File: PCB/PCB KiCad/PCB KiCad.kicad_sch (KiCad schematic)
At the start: 0 parts

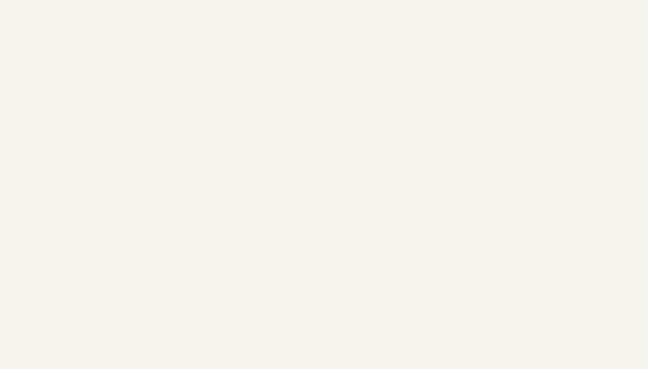
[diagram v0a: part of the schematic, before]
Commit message: draw schematic for 60%
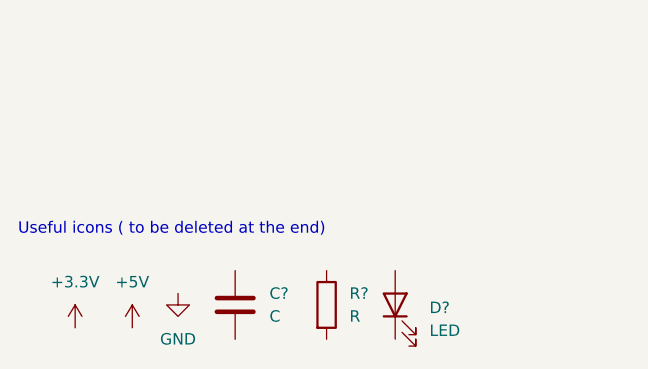
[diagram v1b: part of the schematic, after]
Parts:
- added C?: C, Capacitor_SMD:C_0805_2012Metric_Pad1.18x1.45mm_HandSolder, symbol Device:C
- added D?: LED, symbol Device:LED
- added R?: R, Resistor_SMD:R_0805_2012Metric_Pad1.20x1.40mm_HandSolder, symbol Device:R
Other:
- note added: "Useful icons ( to be deleted at the end)"

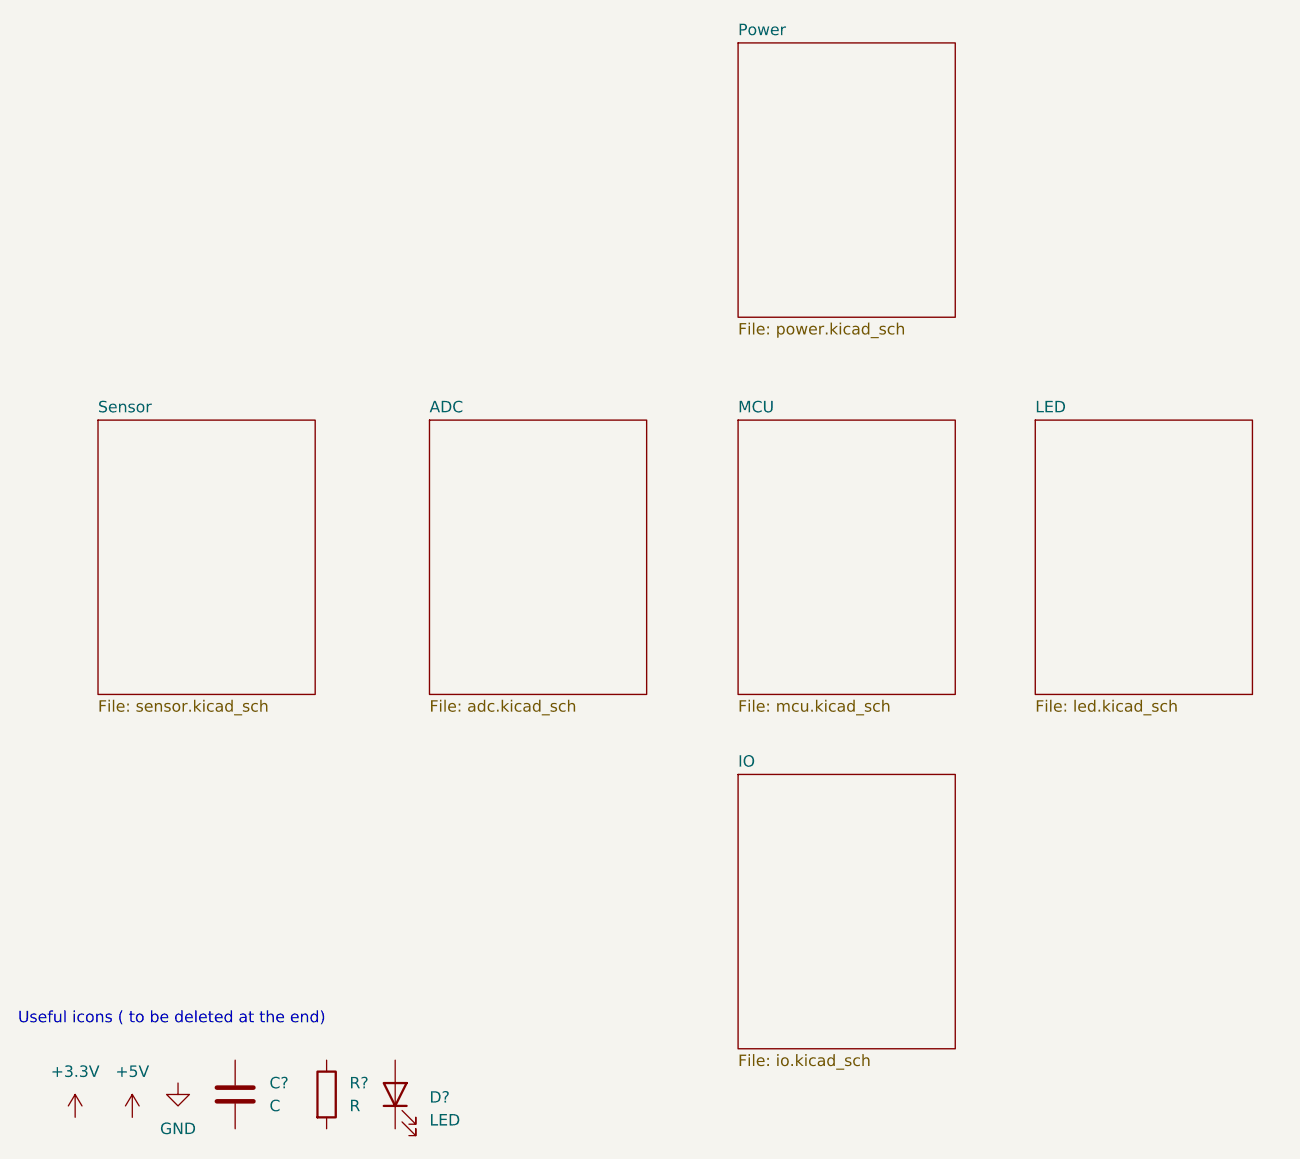
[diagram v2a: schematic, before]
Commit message: Merge MCU and IO into single sheet, wire LEDs
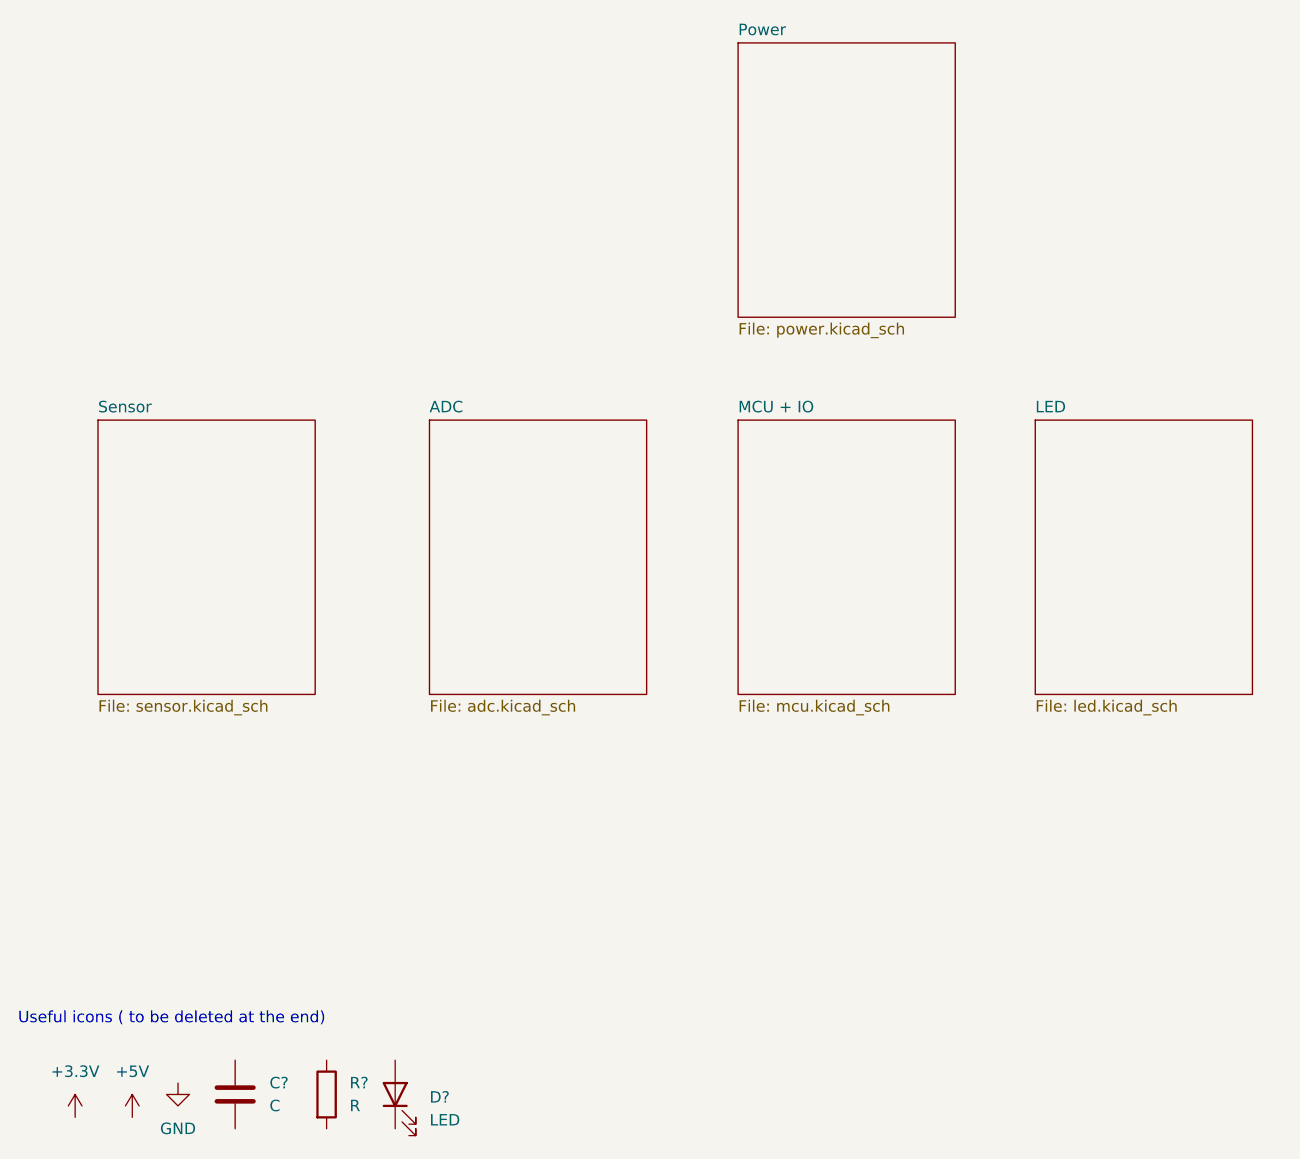
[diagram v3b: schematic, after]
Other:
- sheet MCU renamed MCU + IO
- removed sheet IO
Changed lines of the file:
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@@
     (pin "1")
   )
-  (sheet (at 139.7 116.84) (size 24.13 30.48) (fields_autoplaced)
-    (stroke (width 0.1524) (type solid) (color 0 0 0 0))
-    (fill (color 0 0 0 0.0000))
-    (property "Sheet name" "IO" (id 0) (at 139.7 116.1284 0)
-      (effects (font (size 1.27 1.27)) (justify left bottom))
-    )
-    (property "Sheet file" "io.kicad_sch" (id 1) (at 139.7 147.9046 0)
-      (effects (font (size 1.27 1.27)) (justify left top))
-    )
-  )
   (sheet (at 172.72 77.47) (size 24.13 30.48) (fields_autoplaced)
     (stroke (width 0.1524) (type solid) (color 0 0 0 0))
@@
     (stroke (width 0.1524) (type solid) (color 0 0 0 0))
     (fill (color 0 0 0 0.0000))
-    (property "Sheet name" "MCU" (id 0) (at 139.7 76.7584 0)
+    (property "Sheet name" "MCU + IO" (id 0) (at 139.7 76.7584 0)
       (effects (font (size 1.27 1.27)) (justify left bottom))
     )
@@
     (path "/5869e7b3-0d61-455b-97ad-e4e8b4829f27" (page "5"))
     (path "/2f10b7a1-df61-45b4-9fd1-1ebf21b41a15" (page "6"))
-    (path "/044ed909-8654-4432-ad65-2607224e408b" (page "7"))
   )
   (symbol_instances
@@
       (reference "#PWR?") (unit 1) (value "GND") (footprint "")
     )
-    (path "/044ed909-8654-4432-ad65-2607224e408b/21ec72d9-1124-42c2-9fc7-eb24ad0f4d51"
+    (path "/f3879066-a91b-415e-b241-18f9d05de4a2/1ee6cbb1-3bcf-4f52-ae17-38d58ded9eac"
       (reference "#PWR?") (unit 1) (value "+5V") (footprint "")
     )
@@
       (reference "#PWR?") (unit 1) (value "GND") (footprint "")
     )
+    (path "/f3879066-a91b-415e-b241-18f9d05de4a2/3295ec6f-d9f8-4131-ac18-9460a5e4ec20"
+      (reference "#PWR?") (unit 1) (value "GND") (footprint "")
+    )
     (path "/33859785-1c1f-4d76-97ab-2edbd3c62d44"
       (reference "#PWR?") (unit 1) (value "+5V") (footprint "")
@@
       (reference "#PWR?") (unit 1) (value "+5V") (footprint "")
     )
-    (path "/044ed909-8654-4432-ad65-2607224e408b/44cb886f-3f45-459c-bb63-d8fa7feca2cc"
-      (reference "#PWR?") (unit 1) (value "GND") (footprint "")
+    (path "/f3879066-a91b-415e-b241-18f9d05de4a2/3eae3c53-6c22-41a2-8188-cb892adb04bd"
+      (reference "#PWR?") (unit 1) (value "+3.3V") (footprint "")
     )
     (path "/2f10b7a1-df61-45b4-9fd1-1ebf21b41a15/5a3162c0-f15e-448b-abae-45969abc5e29"
@@
     (path "/a8dcb7a4-48cf-403e-b881-d44234291c62/5acc43a2-ea8d-401d-9505-8135b0ac4f98"
       (reference "#PWR?") (unit 1) (value "+5V") (footprint "")
+    )
+    (path "/f3879066-a91b-415e-b241-18f9d05de4a2/5ba1661a-f966-4972-b9eb-8ebbb748d9d2"
+      (reference "#PWR?") (unit 1) (value "GND") (footprint "")
     )
     (path "/5869e7b3-0d61-455b-97ad-e4e8b4829f27/62d01918-163e-47c7-9243-aba22cda7aea"
@@
       (reference "#PWR?") (unit 1) (value "GND") (footprint "")
     )
-    (path "/044ed909-8654-4432-ad65-2607224e408b/adcb9bf2-9ca9-4769-8fd9-25b74705c77d"
-      (reference "#PWR?") (unit 1) (value "+3.3V") (footprint "")
-    )
     (path "/2f10b7a1-df61-45b4-9fd1-1ebf21b41a15/afd8a72b-4a58-4167-a551-15d1a3583d2c"
       (reference "#PWR?") (unit 1) (value "+3.3V") (footprint "")
     )
-    (path "/044ed909-8654-4432-ad65-2607224e408b/b07b9ef8-d0ce-4207-83c5-54e0af2aa6ed"
-      (reference "#PWR?") (unit 1) (value "+5V") (footprint "")
+    (path "/f3879066-a91b-415e-b241-18f9d05de4a2/b4d64565-70f6-4b51-9fe4-c5ff18595970"
+      (reference "#PWR?") (unit 1) (value "GND") (footprint "")
     )
     (path "/5869e7b3-0d61-455b-97ad-e4e8b4829f27/b8735049-b724-48b3-bf95-7a67e3592f22"
-      (reference "#PWR?") (unit 1) (value "GND") (footprint "")
-    )
-    (path "/044ed909-8654-4432-ad65-2607224e408b/b8c5e5cf-36b8-4473-88d0-ee6b7dc8ed59"
       (reference "#PWR?") (unit 1) (value "GND") (footprint "")
     )
@@
       (reference "#PWR?") (unit 1) (value "+2V5") (footprint "")
     )
-    (path "/044ed909-8654-4432-ad65-2607224e408b/cedefae5-afc3-4859-92fa-f02818664f67"
-      (reference "#PWR?") (unit 1) (value "GND") (footprint "")
+    (path "/f3879066-a91b-415e-b241-18f9d05de4a2/d39bcc69-25d4-4cfd-a423-8711822048d2"
+      (reference "#PWR?") (unit 1) (value "+5V") (footprint "")
     )
     (path "/a8dcb7a4-48cf-403e-b881-d44234291c62/d8656ed6-fa93-4312-9d18-e136dfd8bf41"
       (reference "#PWR?") (unit 1) (value "GND") (footprint "")
     )
+    (path "/f3879066-a91b-415e-b241-18f9d05de4a2/f4ed2dcb-a307-413c-a4b4-734b0d790e50"
+      (reference "#PWR?") (unit 1) (value "GND") (footprint "")
+    )
     (path "/5869e7b3-0d61-455b-97ad-e4e8b4829f27/f8932546-4a79-4528-803c-5677b8a9bafb"
       (reference "#PWR?") (unit 1) (value "GND") (footprint "")
@@
     (path "/2f10b7a1-df61-45b4-9fd1-1ebf21b41a15/fa88dfc7-3db5-45b5-b84e-e8def18ec096"
       (reference "#PWR?") (unit 1) (value "+3.3V") (footprint "")
-    )
-    (path "/044ed909-8654-4432-ad65-2607224e408b/fb743507-086d-4b57-97a7-10a4ea1fbfcc"
-      (reference "#PWR?") (unit 1) (value "GND") (footprint "")
     )
     (path "/a8dcb7a4-48cf-403e-b881-d44234291c62/ff23efb8-153d-4afb-b85c-c4e507f3b942"
@@
       (reference "C?") (unit 1) (value "100n") (footprint "")
     )
-    (path "/044ed909-8654-4432-ad65-2607224e408b/058d18df-79d7-4ae0-82d1-394d1873b4d4"
-      (reference "D?") (unit 1) (value "LED") (footprint "")
+    (path "/f3879066-a91b-415e-b241-18f9d05de4a2/10524258-bfb6-4675-b62a-82562d6aed47"
+      (reference "D?") (unit 1) (value "LED RED") (footprint "")
     )
     (path "/2f10b7a1-df61-45b4-9fd1-1ebf21b41a15/1ea65141-3dcf-4489-9028-27f756bf783f"
@@
       (reference "D?") (unit 1) (value "LED") (footprint "LED_SMD:LED_1206_3216Metric_Pad1.42x1.75mm_HandSolder")
     )
+    (path "/f3879066-a91b-415e-b241-18f9d05de4a2/998d123c-4a0f-4c5d-a916-76e1efcee63d"
+      (reference "D?") (unit 1) (value "LED BLUE") (footprint "")
+    )
     (path "/2f10b7a1-df61-45b4-9fd1-1ebf21b41a15/ae6de9b9-0550-4376-b49b-7259989631bc"
       (reference "D?") (unit 1) (value "LED") (footprint "LED_SMD:LED_1206_3216Metric_Pad1.42x1.75mm_HandSolder")
-    )
-    (path "/044ed909-8654-4432-ad65-2607224e408b/b282bd33-79d8-40ba-ae5f-2934b60c9c1f"
-      (reference "D?") (unit 1) (value "LED") (footprint "")
     )
     (path "/2f10b7a1-df61-45b4-9fd1-1ebf21b41a15/cc16645b-47f5-4a9d-a523-9327722646b2"
@@
       (reference "R?") (unit 1) (value "49.9") (footprint "Resistor_SMD:R_0805_2012Metric_Pad1.20x1.40mm_HandSolder")
     )
-    (path "/044ed909-8654-4432-ad65-2607224e408b/1b20cbe8-c1a1-4157-a6cf-bfabdd184c92"
-      (reference "R?") (unit 1) (value "10k") (footprint "")
-    )
     (path "/2f10b7a1-df61-45b4-9fd1-1ebf21b41a15/1e782a0c-d936-440f-8252-000daab275a0"
       (reference "R?") (unit 1) (value "0") (footprint "Resistor_SMD:R_0805_2012Metric_Pad1.20x1.40mm_HandSolder")
@@
       (reference "R?") (unit 1) (value "1k") (footprint "Resistor_SMD:R_0805_2012Metric_Pad1.20x1.40mm_HandSolder")
     )
+    (path "/f3879066-a91b-415e-b241-18f9d05de4a2/6941070f-e7e2-4854-a029-3c08105a8b72"
+      (reference "R?") (unit 1) (value "10k") (footprint "")
+    )
     (path "/a8dcb7a4-48cf-403e-b881-d44234291c62/6e050f2e-304d-4f13-9dfd-871a6091f20f"
       (reference "R?") (unit 1) (value "10k") (footprint "")
@@
       (reference "R?") (unit 1) (value "100") (footprint "")
     )
-    (path "/044ed909-8654-4432-ad65-2607224e408b/790d7e3d-277a-4b91-a810-db56947153bd"
-      (reference "R?") (unit 1) (value "10k") (footprint "")
+    (path "/f3879066-a91b-415e-b241-18f9d05de4a2/7115ca8a-847a-43d2-ad8b-b7553ea695b3"
+      (reference "R?") (unit 1) (value "100") (footprint "")
     )
     (path "/a8dcb7a4-48cf-403e-b881-d44234291c62/8008c118-17d6-4e79-95d5-baa16a155af9"
       (reference "R?") (unit 1) (value "49.9") (footprint "Resistor_SMD:R_0805_2012Metric_Pad1.20x1.40mm_HandSolder")
     )
+    (path "/f3879066-a91b-415e-b241-18f9d05de4a2/895617d2-1039-4d00-af23-a2811e8c17e3"
+      (reference "R?") (unit 1) (value "82") (footprint "")
+    )
     (path "/2f10b7a1-df61-45b4-9fd1-1ebf21b41a15/96b18e64-1a9b-480e-892f-16872ba9575b"
       (reference "R?") (unit 1) (value "0") (footprint "Resistor_SMD:R_0805_2012Metric_Pad1.20x1.40mm_HandSolder")
@@
       (reference "R?") (unit 1) (value "0") (footprint "")
     )
+    (path "/f3879066-a91b-415e-b241-18f9d05de4a2/d3b873a8-4632-45d2-8ffa-a1779cde7433"
+      (reference "R?") (unit 1) (value "10k") (footprint "")
+    )
     (path "/98df1e87-3735-4cb9-8253-663f6eb2234f/dc7e688a-de01-4f67-ae8e-7f7e60e60ade"
       (reference "R?") (unit 1) (value "301") (footprint "")
@@
       (reference "R?") (unit 1) (value "43") (footprint "Resistor_SMD:R_0805_2012Metric_Pad1.20x1.40mm_HandSolder")
     )
-    (path "/044ed909-8654-4432-ad65-2607224e408b/506a1fdf-3e24-4a05-833a-02fd40376986"
+    (path "/f3879066-a91b-415e-b241-18f9d05de4a2/3b268a0c-2c7e-4464-bfbe-f32e2fc2a84c"
+      (reference "SW?") (unit 1) (value "MCU_RESET") (footprint "")
+    )
+    (path "/f3879066-a91b-415e-b241-18f9d05de4a2/7621086c-9e5c-4d01-a159-6ac8ec504518"
       (reference "SW?") (unit 1) (value "TRIGGER") (footprint "")
     )
-    (path "/044ed909-8654-4432-ad65-2607224e408b/fcf506b3-9cd7-4184-ba08-b21d460904f1"
-      (reference "SW?") (unit 1) (value "MCU_RESET") (footprint "")
-    )
     (path "/5869e7b3-0d61-455b-97ad-e4e8b4829f27/15d68d93-0044-44e2-8500-ef5c5b041700"

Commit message: first check + add connectors
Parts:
- removed C?: C, Capacitor_SMD:C_0805_2012Metric_Pad1.18x1.45mm_HandSolder, symbol Device:C
- removed D?: LED, symbol Device:LED
- removed R?: R, Resistor_SMD:R_0805_2012Metric_Pad1.20x1.40mm_HandSolder, symbol Device:R
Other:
- note removed: "Useful icons ( to be deleted at the end)"

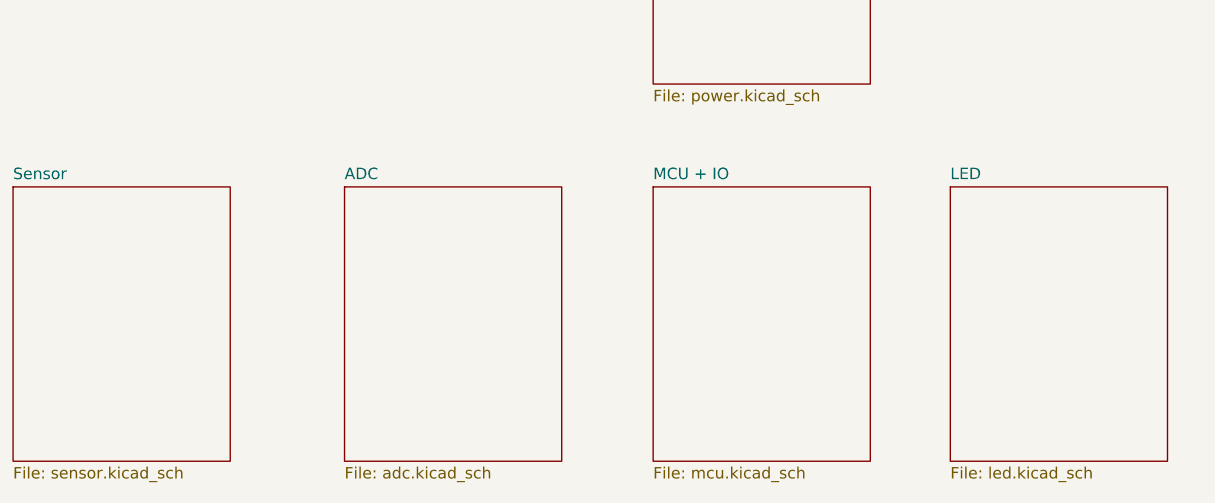
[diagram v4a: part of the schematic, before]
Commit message: ERC: add power flags to satisfy the ERC crap
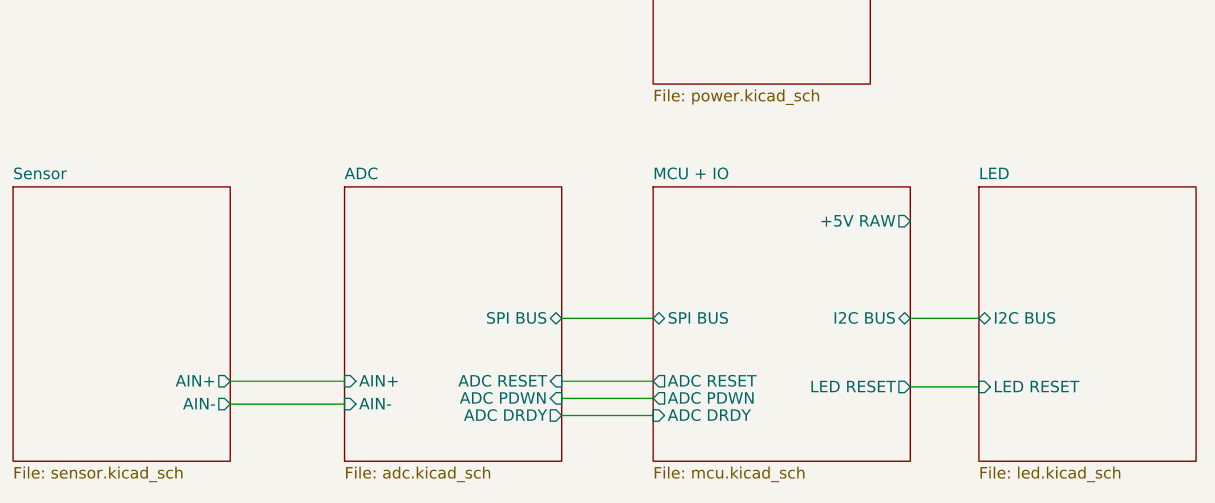
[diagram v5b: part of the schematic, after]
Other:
- sheet ADC ports: added ADC DRDY, ADC PDWN, ADC RESET, AIN+, AIN-, SPI BUS; removed none
- sheet LED ports: added I2C BUS, LED RESET; removed none
- sheet MCU + IO ports: added +5V RAW, ADC DRDY, ADC PDWN, ADC RESET, I2C BUS, LED RESET, SPI BUS; removed none
- sheet Sensor ports: added AIN+, AIN-; removed none
